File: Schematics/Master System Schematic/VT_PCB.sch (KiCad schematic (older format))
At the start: 34 parts, among them K13 Voltage Tap Relay, K14 Voltage Tap Relay, K15 Voltage Tap Relay, K16 Voltage Tap Relay, K17 Voltage Tap Relay, K18 Voltage Tap Relay, K19 Voltage Tap Relay, K20 Voltage Tap Relay, K21 Voltage Tap Relay, K22 Voltage Tap Relay

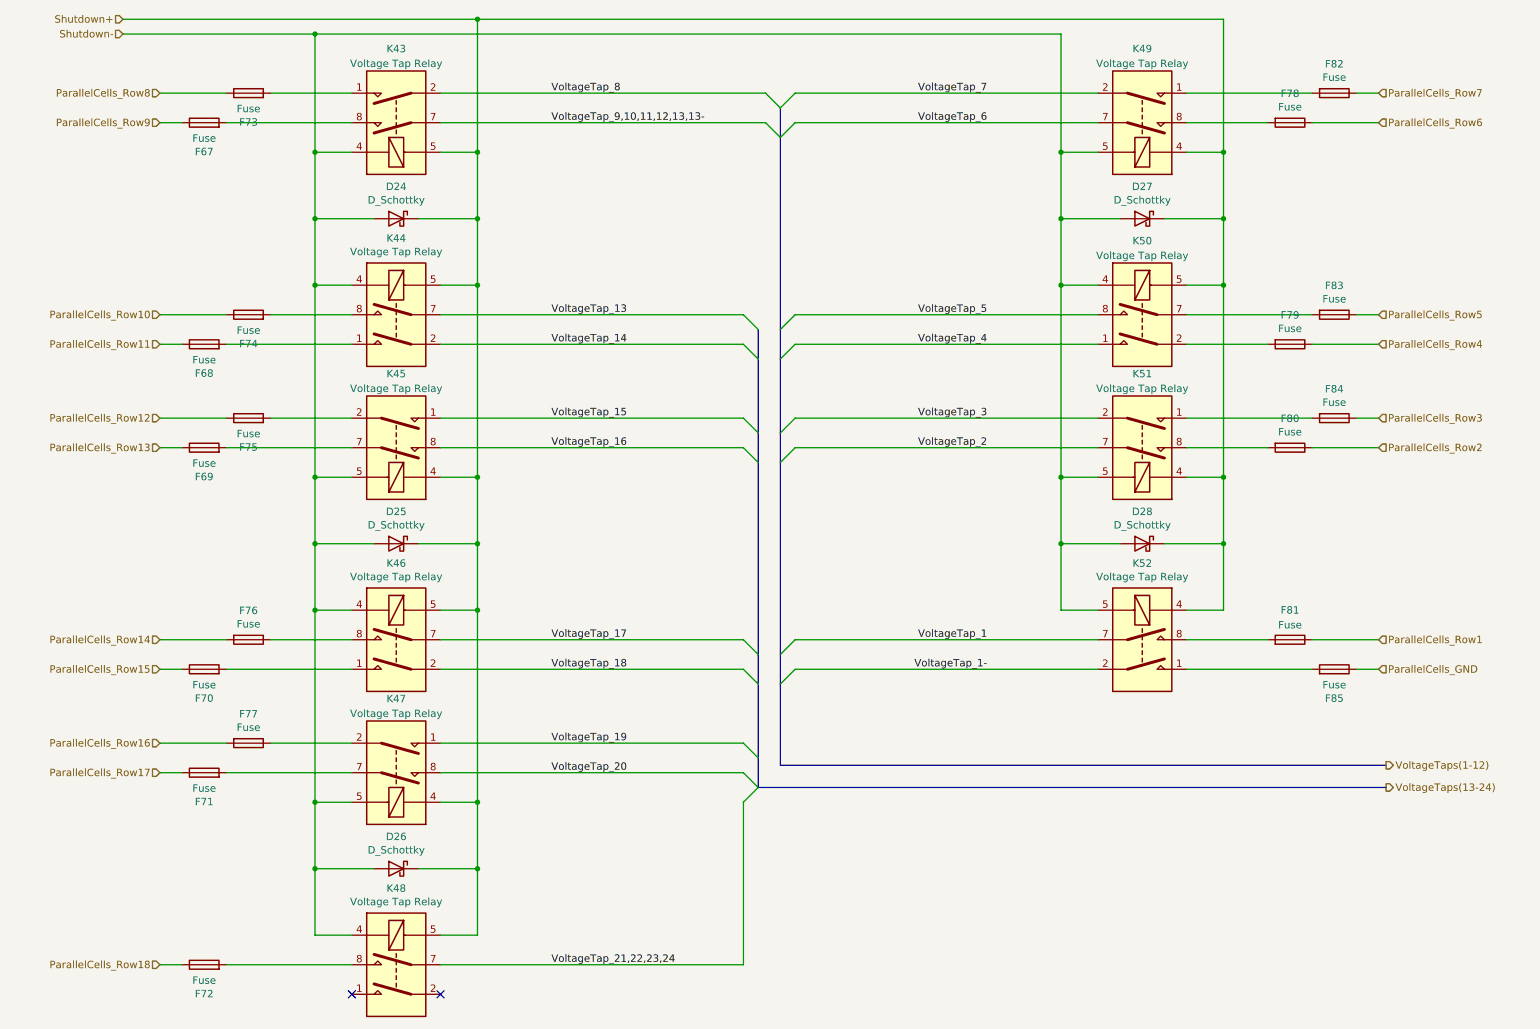
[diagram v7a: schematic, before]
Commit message: Segment Layer
> Added segments to Segment_Layer sheet
> Added VT PCBs and Thermistor PCBs to Segment_Layer sheet
> Removed relays from VT PCBs
> Still need to add connectors to VT and Thermistor PCBs once PCBs have been redesigned
> Added outputs for Segment_Layer sheet
> Added wire gauges to Segment_Layer sheet

Segment_Layer V1.0
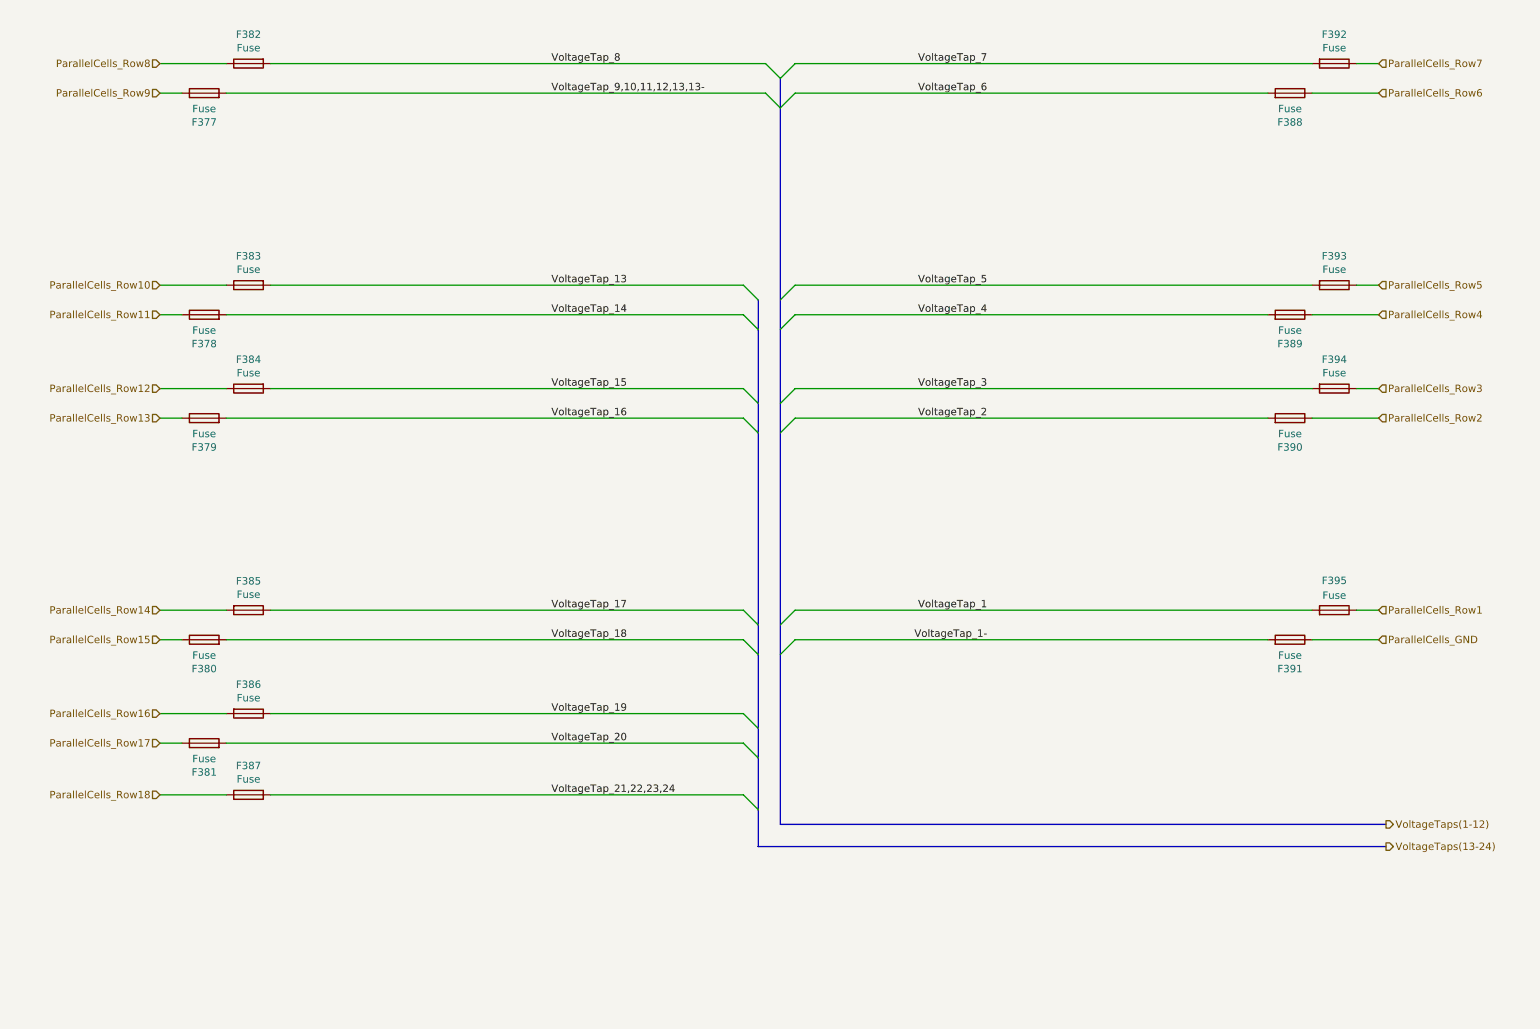
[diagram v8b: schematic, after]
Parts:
- removed D10, D11, D12, D13, D9: D_Schottky, symbol Device:D_Schottky
- removed K13, K14, K15, K16, K17, K18, K19, K20, K21, K22: Voltage Tap Relay, Relay_THT:Relay_DPST_Fujitsu_FTR-F1A, symbol Relay:Fujitsu_FTR-F1A
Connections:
- net VoltageTap_1: now also F24.2
- net VoltageTap_1-: now also F28.2
- net VoltageTap_13: now also F17.2
- net VoltageTap_14: now also F11.2
- net VoltageTap_15: now also F18.2
- net VoltageTap_16: now also F12.2
- net VoltageTap_17: now also F19.1
- net VoltageTap_18: now also F13.2
- net VoltageTap_19: now also F20.1
- net VoltageTap_2: now also F23.2
- net VoltageTap_20: now also F14.2
- net VoltageTap_21,22,23,24: now also F15.2
- net VoltageTap_3: now also F27.2
- net VoltageTap_4: now also F22.2
- net VoltageTap_5: now also F26.2
- net VoltageTap_6: now also F21.2
- net VoltageTap_7: now also F25.2
- net VoltageTap_8: now also F16.2
- net VoltageTap_9,10,11,12,13,13-: now also F10.2
- no-connect marks 2 -> 0
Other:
- moved on the sheet: F377, F378, F379, F380, F381, F382, F383, F384, F385, F386, F387, F388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
